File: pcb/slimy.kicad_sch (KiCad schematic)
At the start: 99 parts, among them K1 KEYSW, K10 KEYSW, K11 KEYSW, K12 KEYSW, K13 KEYSW, K14 KEYSW, K15 KEYSW, K16 KEYSW, K17 KEYSW, K18 KEYSW, K19 KEYSW, K2 KEYSW, K20 KEYSW, K21 KEYSW, K22 KEYSW, K23 KEYSW, K24 KEYSW, K25 KEYSW, K26 KEYSW, K27 KEYSW, K28 KEYSW, K29 KEYSW, K3 KEYSW, K30 KEYSW, K31 KEYSW, K32 KEYSW, K33 KEYSW, K34 KEYSW, K35 KEYSW, K36 KEYSW, K37 KEYSW, K38 KEYSW, K39 KEYSW, K4 KEYSW, K40 KEYSW, K41 KEYSW, K42 KEYSW, K43 KEYSW, K44 KEYSW, K45 KEYSW, K46 KEYSW, K47 KEYSW, K48 KEYSW, K5 KEYSW, K6 KEYSW, K7 KEYSW, K8 KEYSW, K9 KEYSW, U1 Teensy3.2, U2 ST7789_SPI, U3 PIM447

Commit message: Cleanup
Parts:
- U1: footprint teensy:Teensy30_31_32_All_Pins -> my_lib:Teensy32
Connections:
- net Col11: no longer U1.29 (22_A8_Touch_PWM)
- net Col12: no longer U1.30 (23_A9_Touch_PWM)
- net VCC: no longer U1.33 (Vin)
- no-connect marks 0 -> 33
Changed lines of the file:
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@@
 (kicad_sch (version 20211123) (generator eeschema)
   (paper "A3")
-  (junction (at 153.67 105.41) (diameter 0) (color 0 0 0 0)
-  )
   (junction (at 133.35 55.88) (diameter 0) (color 0 0 0 0)
   )
@@
   (junction (at 153.67 64.77) (diameter 0) (color 0 0 0 0)
   )
-  (junction (at 287.02 105.41) (diameter 0) (color 0 0 0 0)
-  )
   (junction (at 233.68 64.77) (diameter 0) (color 0 0 0 0)
   )
@@
   (junction (at 287.02 44.45) (diameter 0) (color 0 0 0 0)
   )
-  (junction (at 207.01 105.41) (diameter 0) (color 0 0 0 0)
-  )
   (junction (at 293.37 96.52) (diameter 0) (color 0 0 0 0)
   )
@@
   (junction (at 340.36 85.09) (diameter 0) (color 0 0 0 0)
   )
-  (junction (at 233.68 105.41) (diameter 0) (color 0 0 0 0)
-  )
   (junction (at 80.01 116.84) (diameter 0) (color 0 0 0 0)
   )
@@
   (junction (at 73.66 44.45) (diameter 0) (color 0 0 0 0)
   )
-  (junction (at 260.35 105.41) (diameter 0) (color 0 0 0 0)
-  )
   (junction (at 260.35 44.45) (diameter 0) (color 0 0 0 0)
   )
@@
   (junction (at 133.35 96.52) (diameter 0) (color 0 0 0 0)
   )
-  (junction (at 180.34 105.41) (diameter 0) (color 0 0 0 0)
-  )
   (junction (at 106.68 96.52) (diameter 0) (color 0 0 0 0)
   )
   (junction (at 214.63 243.84) (diameter 0) (color 0 0 0 0)
   )
+  (no_connect (at 151.13 224.79))
+  (no_connect (at 214.63 236.22))
+  (no_connect (at 167.64 245.11))
+  (no_connect (at 151.13 256.54))
+  (no_connect (at 88.9 267.97))
+  (no_connect (at 88.9 270.51))
+  (no_connect (at 88.9 255.27))
+  (no_connect (at 88.9 257.81))
+  (no_connect (at 88.9 260.35))
+  (no_connect (at 88.9 262.89))
+  (no_connect (at 38.1 255.27))
+  (no_connect (at 38.1 252.73))
+  (no_connect (at 38.1 250.19))
+  (no_connect (at 38.1 247.65))
+  (no_connect (at 38.1 242.57))
+  (no_connect (at 38.1 245.11))
+  (no_connect (at 88.9 219.71))
+  (no_connect (at 88.9 222.25))
+  (no_connect (at 88.9 224.79))
+  (no_connect (at 88.9 227.33))
+  (no_connect (at 88.9 229.87))
+  (no_connect (at 88.9 232.41))
+  (no_connect (at 88.9 234.95))
+  (no_connect (at 88.9 237.49))
+  (no_connect (at 88.9 240.03))
+  (no_connect (at 88.9 242.57))
+  (no_connect (at 88.9 245.11))
+  (no_connect (at 88.9 247.65))
+  (no_connect (at 88.9 207.01))
+  (no_connect (at 88.9 209.55))
+  (no_connect (at 88.9 212.09))
+  (no_connect (at 88.9 214.63))
+  (no_connect (at 88.9 217.17))
   (wire (pts (xy 266.7 85.09) (xy 271.78 85.09))
     (stroke (width 0) (type default) (color 0 0 0 0))
@@
     (stroke (width 0) (type default) (color 0 0 0 0))
   )
-  (wire (pts (xy 153.67 105.41) (xy 153.67 125.73))
-    (stroke (width 0) (type default) (color 0 0 0 0))
-  )
   (wire (pts (xy 160.02 64.77) (xy 165.1 64.77))
     (stroke (width 0) (type default) (color 0 0 0 0))
@@
     (stroke (width 0) (type default) (color 0 0 0 0))
   )
-  (wire (pts (xy 180.34 105.41) (xy 180.34 125.73))
-    (stroke (width 0) (type default) (color 0 0 0 0))
-  )
   (wire (pts (xy 35.56 224.79) (xy 38.1 224.79))
     (stroke (width 0) (type default) (color 0 0 0 0))
@@
     (stroke (width 0) (type default) (color 0 0 0 0))
   )
-  (wire (pts (xy 287.02 105.41) (xy 287.02 125.73))
-    (stroke (width 0) (type default) (color 0 0 0 0))
-  )
   (wire (pts (xy 35.56 270.51) (xy 38.1 270.51))
     (stroke (width 0) (type default) (color 0 0 0 0))
@@
     (stroke (width 0) (type default) (color 0 0 0 0))
   )
-  (wire (pts (xy 207.01 105.41) (xy 207.01 125.73))
-    (stroke (width 0) (type default) (color 0 0 0 0))
-  )
   (wire (pts (xy 230.378 237.49) (xy 232.664 237.49))
     (stroke (width 0) (type default) (color 0 0 0 0))
@@
     (stroke (width 0) (type default) (color 0 0 0 0))
   )
-  (wire (pts (xy 260.35 105.41) (xy 260.35 125.73))
-    (stroke (width 0) (type default) (color 0 0 0 0))
-  )
   (wire (pts (xy 73.66 24.13) (xy 73.66 44.45))
     (stroke (width 0) (type default) (color 0 0 0 0))
@@
     (stroke (width 0) (type default) (color 0 0 0 0))
   )
-  (wire (pts (xy 233.68 105.41) (xy 233.68 125.73))
-    (stroke (width 0) (type default) (color 0 0 0 0))
-  )
   (wire (pts (xy 240.03 68.58) (xy 240.03 64.77))
     (stroke (width 0) (type default) (color 0 0 0 0))
@@
       (effects (font (size 1.524 1.524)))
     )
-    (property "Footprint" "teensy:Teensy30_31_32_All_Pins" (id 2) (at 63.5 260.35 0)
+    (property "Footprint" "my_lib:Teensy32" (id 2) (at 63.5 260.35 0)
       (effects (font (size 1.524 1.524)) hide)
     )
@@
     (pin "27")
     (pin "28")
-    (pin "29")
     (pin "3")
-    (pin "30")
-    (pin "31")
-    (pin "32")
-    (pin "33")
-    (pin "34")
-    (pin "35")
-    (pin "36")
-    (pin "37")
-    (pin "38")
-    (pin "39")
     (pin "4")
-    (pin "40")
-    (pin "41")
-    (pin "42")
-    (pin "43")
-    (pin "44")
-    (pin "45")
-    (pin "46")
-    (pin "47")
-    (pin "48")
-    (pin "49")
     (pin "5")
-    (pin "50")
-    (pin "51")
-    (pin "52")
-    (pin "53")
-    (pin "54")
     (pin "6")
     (pin "7")
@@
     )
     (path "/8b349b81-1fe8-4547-b869-c999eefc5c64"
-      (reference "U1") (unit 1) (value "Teensy3.2") (footprint "teensy:Teensy30_31_32_All_Pins")
+      (reference "U1") (unit 1) (value "Teensy3.2") (footprint "my_lib:Teensy32")
     )
     (path "/eee9a983-2df4-4be4-87a4-475f2257b1be"

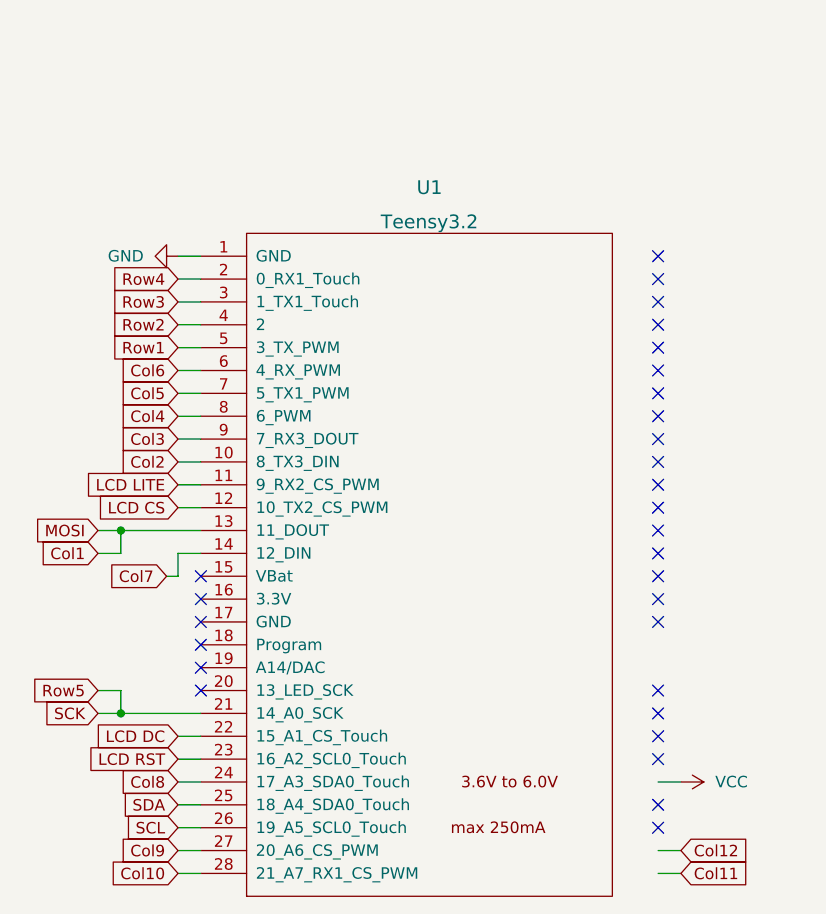
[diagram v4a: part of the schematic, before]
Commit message: Fix issues with updated pins
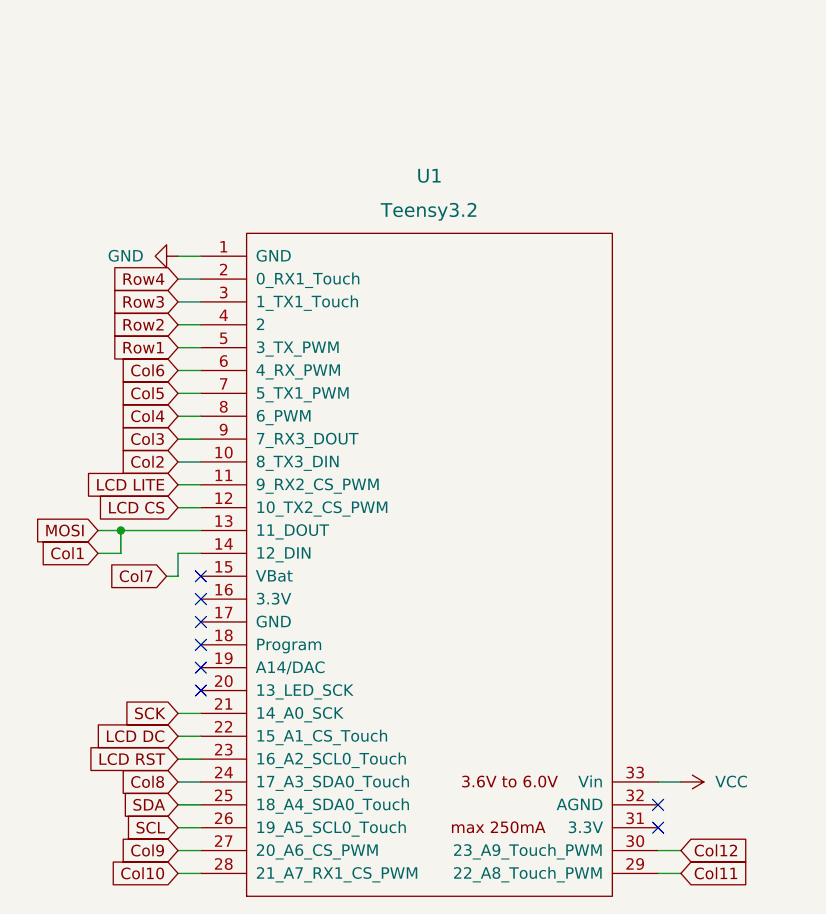
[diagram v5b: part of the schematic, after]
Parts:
- K1, K10, K11, K12, K13, K14, K15, K16, K17, K18, K19, K2, K20, K21, K22, K23, K24, K25, K26, K27, K28, K29, K3, K30, K31, K32, K33, K34, K35, K36, K37, K38, K39, K4, K40, K41, K42, K43, K44, K45, K46, K47, K48, K5, K6, K7, K8, K9: footprint (none) -> my_lib:MX-1U-Hotswap-Antishear-flipped
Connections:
- net Col11: now also U1.29 (22_A8_Touch_PWM)
- net Col12: now also U1.30 (23_A9_Touch_PWM)
- net VCC: now also U1.33 (Vin)
- net Row5 renamed SCK
- no-connect marks 33 -> 12

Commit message: Update diode footprint
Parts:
- D1, D10, D11, D12, D13, D14, D15, D16, D17, D18, D19, D2, D20, D21, D22, D23, D24, D25, D26, D27, D28, D29, D3, D30, D31, D32, D33, D34, D35, D36, D37, D38, D39, D4, D40, D41, D42, D43, D44, D45, D46, D47, D48, D5, D6, D7, D8, D9: footprint my_lib:D_SOD123_axial -> (none)
